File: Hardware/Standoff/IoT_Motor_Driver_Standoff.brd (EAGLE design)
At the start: 32 x 25.6 mm, 2 parts

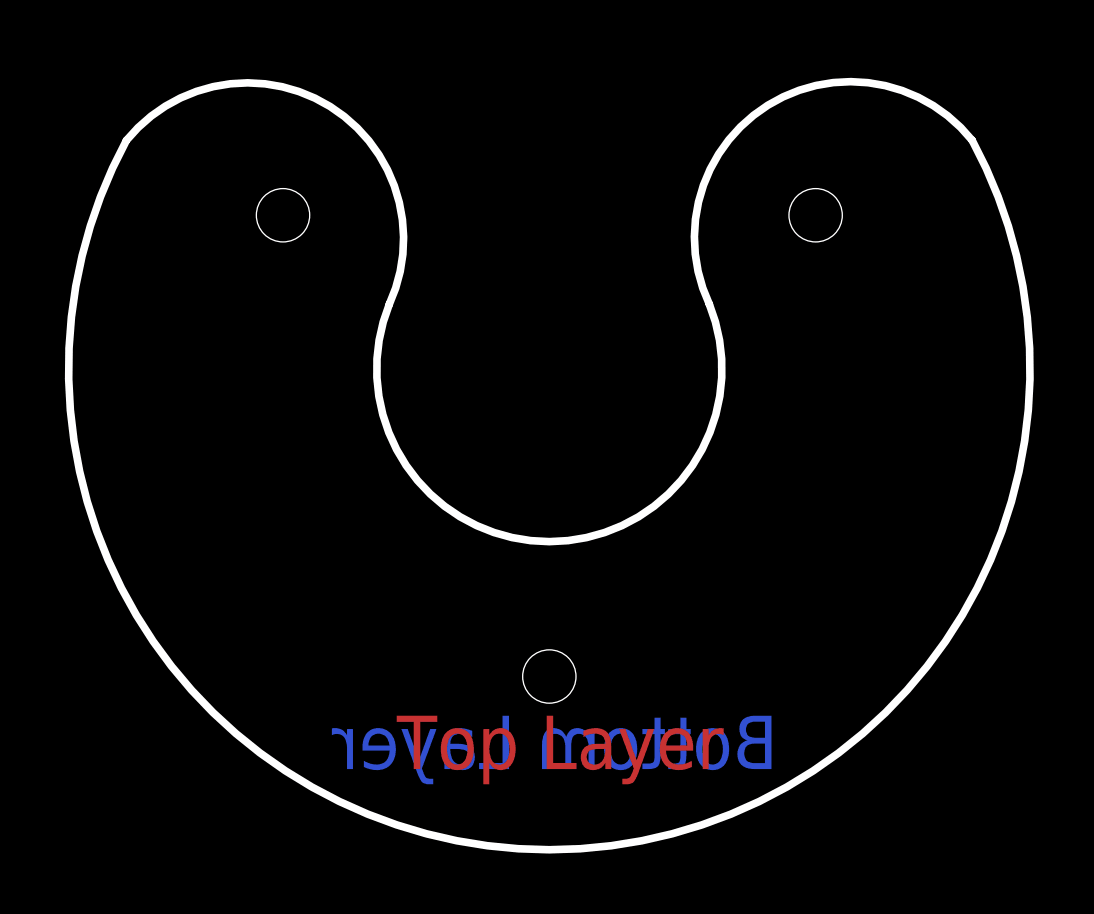
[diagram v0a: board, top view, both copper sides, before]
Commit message: Standoff Updates
Changed the width of the circle for the standoff so there is no friction on the motor when it is spinning. Continued work with layout.
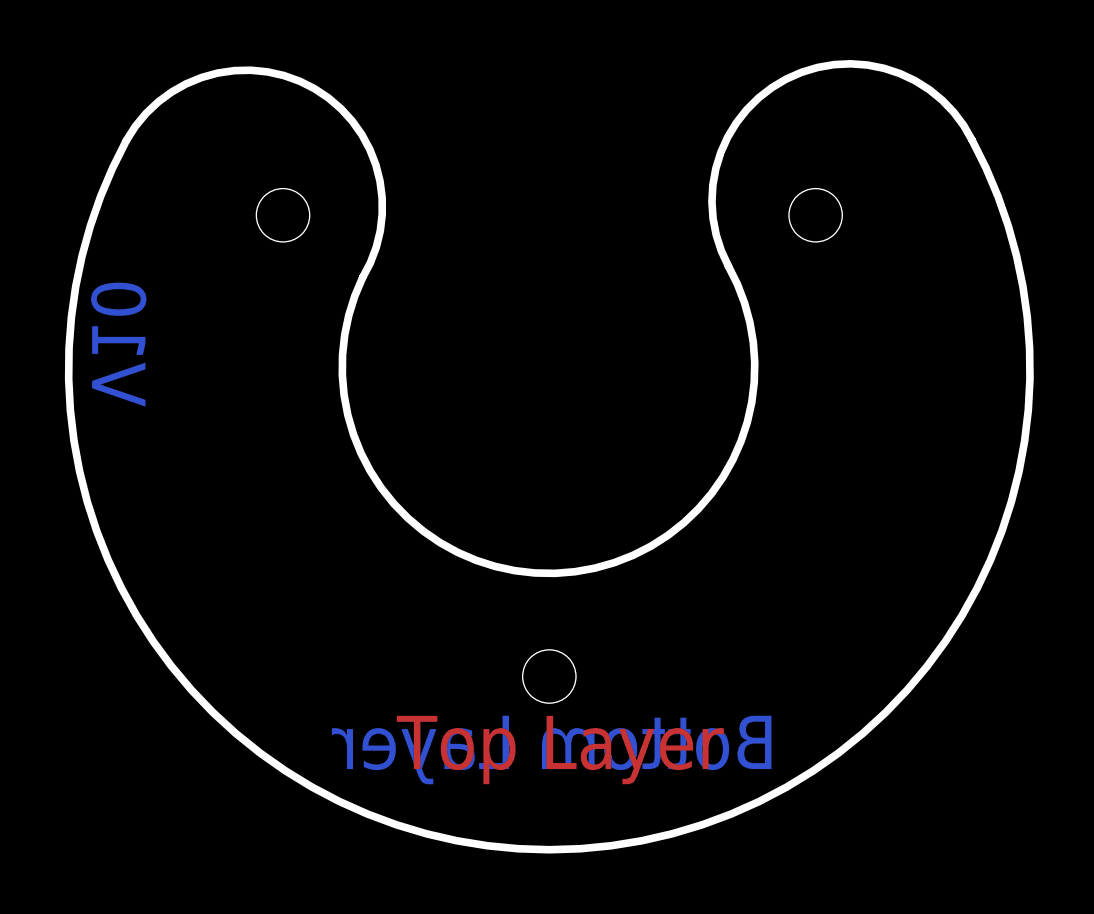
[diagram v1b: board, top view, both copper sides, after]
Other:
- board size 32 x 25.6 mm -> 32 x 26.2 mm
- board text added: "1.2mm Thickness 2-Layer 1oz copper outer 0.5oz copper inner Lead Free HASL"
- board text added: "V10"
- board text removed: "2.2mm Thickness 2-Layer 1oz copper outer 0.5oz copper inner Lead Free HASL"
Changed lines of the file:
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@@
 <text x="-5.08" y="-13.335" size="1.778" layer="1" font="vector" ratio="15">Top Layer</text>
 <text x="7.62" y="-13.335" size="1.778" layer="16" font="vector" ratio="15" rot="MR0">Bottom Layer</text>
-<text x="30.48" y="2.54" size="1.778" layer="51" font="vector">2.2mm Thickness
+<text x="30.48" y="2.54" size="1.778" layer="51" font="vector">1.2mm Thickness
 2-Layer
 1oz copper outer
@@
 Lead Free HASL</text>
 <wire x1="-14.097" y1="7.62" x2="14.097" y2="7.62" width="0.254" layer="20" curve="236.786039"/>
-<wire x1="-14.097" y1="7.62" x2="-5.334" y2="2.159" width="0.254" layer="20" curve="-165.583004"/>
-<wire x1="14.097" y1="7.62" x2="5.334" y2="2.159" width="0.254" layer="20" curve="166.762419"/>
-<wire x1="-5.334" y1="2.159" x2="5.334" y2="2.159" width="0.254" layer="20" curve="224.072454"/>
+<wire x1="-14.097" y1="7.62" x2="-6.223" y2="3.048" width="0.254" layer="20" curve="-182.184611"/>
+<wire x1="14.097" y1="7.62" x2="5.969" y2="3.429" width="0.254" layer="20" curve="182.143584"/>
+<wire x1="-6.223" y1="3.048" x2="5.969" y2="3.429" width="0.254" layer="20" curve="235.037595"/>
+<text x="-15.24" y="-1.27" size="1.778" layer="16" font="vector" ratio="15" rot="MR90">V10</text>
 </plain>
 <attributes>
